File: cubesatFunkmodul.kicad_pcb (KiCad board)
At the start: 4 copper layers, 85 x 85 mm, 96 parts, among them Q1 MMBT5401-TP, Q2 AO3414, Q3 MMBT5551-TP, Q4 MMBT5551-TP, Q5 MMBT5551-TP, Q6 MMBT5551-TP, Q7 MMBT5551-TP, Q8 MMBT5551-TP, U1 MC74HC4538A, U3 ATMEGA128-16AU, U4 LTC3113, U5 RFM23BP, Y1 Crystal_GND24

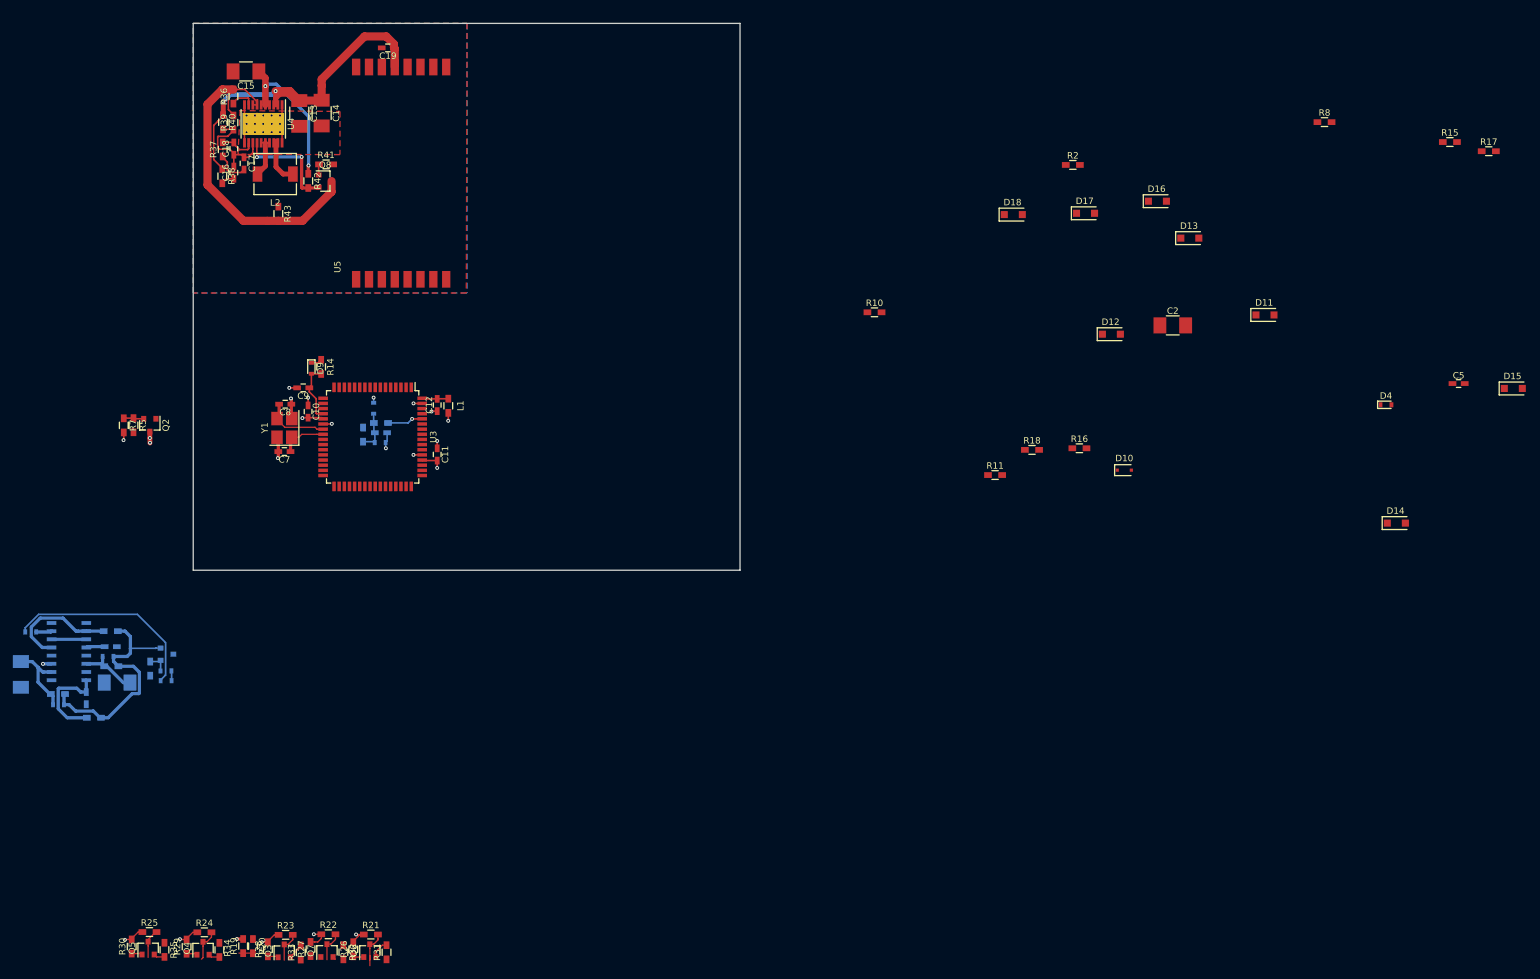
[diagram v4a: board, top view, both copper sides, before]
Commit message: Layout Module1 prefinish
Modules Placed
Ground Plane placed
Supply Plane placed
TODO: Add cubesat connector, Place Antenna connector, Place burnwire connector, Review
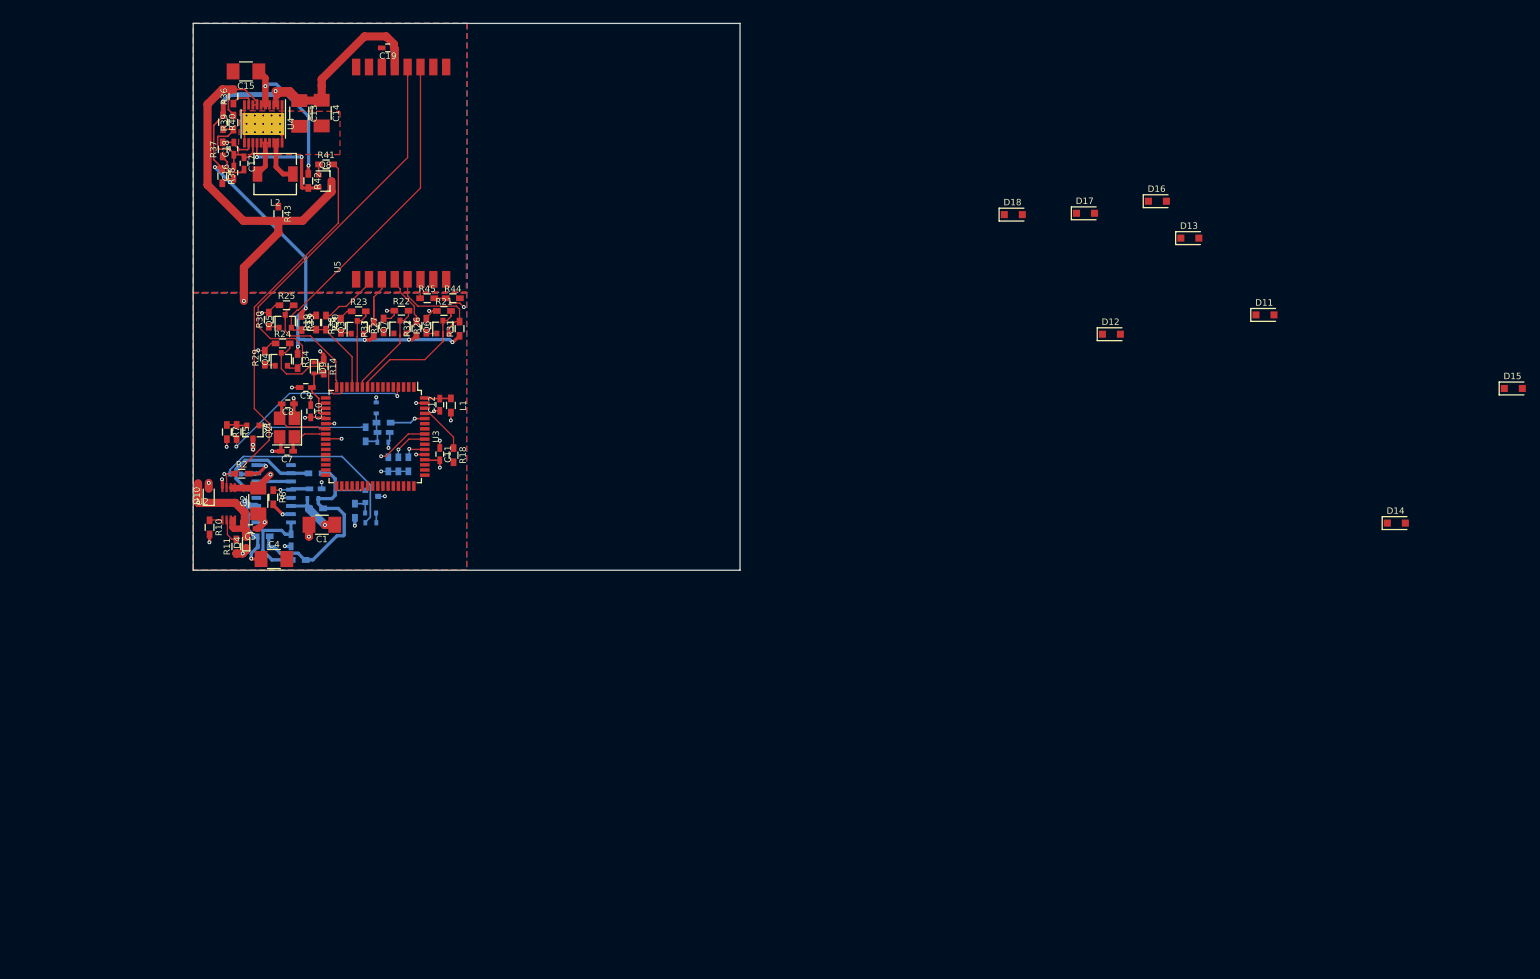
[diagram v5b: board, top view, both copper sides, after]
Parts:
- added R44: 10k, Resistors_SMD:R_0603_HandSoldering, F.Cu at (91.4, 76.7)
- added R45: 4k7, Resistors_SMD:R_0603_HandSoldering, F.Cu at (87.4, 76.7)
- added U2: MAX892, Maxim:µMAX-8, F.Cu at (56.5, 108.6)
- C1, C4: moved to F.Cu
- D1, D2, D3, D4, D5, D6, D7, D8, D9: value STTH102A -> TS4148C
- R15, R16, R17: moved to B.Cu
- moved C5 189.2 mm to (59.9, 112.5), turned to 180 degrees
- moved D4 178.5 mm to (59.2, 114.7), turned to 90 degrees
- moved R17 174.8 mm to (84.5, 102.5), turned to 90 degrees
- moved R8 173.5 mm to (63.4, 107.7), turned to 270 degrees
- moved R15 172.4 mm to (81.3, 102.5), turned to 90 degrees
- moved C2 144.7 mm to (61.1, 108.2), turned to 90 degrees
- moved D10 142.4 mm to (53.4, 107.4), turned to 90 degrees
- moved R2 137.8 mm to (58.5, 104.0)
- moved R11 118.5 mm to (57.7, 115.3), turned to 90 degrees
- moved R10 108.6 mm to (53.5, 112.3), turned to 270 degrees
- moved R16 105.9 mm to (82.9, 102.5), turned to 90 degrees
- moved Q5 99.7 mm to (65.3, 80.3)
- moved R35 99.7 mm to (67.8, 80.6)
- moved R25 99.7 mm to (65.5, 77.8)
- moved R30 99.7 mm to (62.8, 80.1)
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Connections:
- D14 pad 1: (no net) -> /Connector/RX2
- D15 pad 1: (no net) -> /Connector/TX2
- D16 pad 1: (no net) -> /Connector/~ENABLE2~
- R10 pad 1: (no net) -> Net-(R10-Pad1)
- R11 pad 1: (no net) -> /Connector/3.3V
- R11 pad 2: (no net) -> Net-(R11-Pad2)
- U1 pad 9: (no net) -> Net-(U1-Pad9)
- U3 pad 1: (no net) -> Net-(U3-Pad1)
- U3 pad 14: (no net) -> Net-(U3-Pad14)
- U3 pad 17: (no net) -> Net-(U3-Pad17)
- U3 pad 18: (no net) -> Net-(U3-Pad18)
- U3 pad 19: (no net) -> Net-(U3-Pad19)
- U3 pad 26: (no net) -> Net-(U3-Pad26)
- U3 pad 27: (no net) -> Net-(U3-Pad27)
- U3 pad 28: (no net) -> Net-(U3-Pad28)
- U3 pad 29: (no net) -> Net-(U3-Pad29)
- U3 pad 30: (no net) -> Net-(U3-Pad30)
- U3 pad 31: (no net) -> Net-(U3-Pad31)
- U3 pad 32: (no net) -> Net-(U3-Pad32)
- U3 pad 33: (no net) -> Net-(U3-Pad33)
- U3 pad 34: (no net) -> Net-(U3-Pad34)
- U3 pad 35: (no net) -> Net-(U3-Pad35)
- U3 pad 36: (no net) -> Net-(U3-Pad36)
- U3 pad 37: (no net) -> Net-(U3-Pad37)
- U3 pad 38: (no net) -> Net-(U3-Pad38)
- U3 pad 39: (no net) -> Net-(U3-Pad39)
- U3 pad 40: (no net) -> Net-(U3-Pad40)
- U3 pad 41: (no net) -> Net-(U3-Pad41)
- U3 pad 42: (no net) -> Net-(U3-Pad42)
- U3 pad 43: (no net) -> Net-(U3-Pad43)
- U3 pad 44: (no net) -> Net-(U3-Pad44)
- U3 pad 45: (no net) -> Net-(U3-Pad45)
- U3 pad 46: (no net) -> Net-(U3-Pad46)
- U3 pad 47: (no net) -> Net-(U3-Pad47)
- U3 pad 48: (no net) -> Net-(U3-Pad48)
- U3 pad 49: (no net) -> Net-(U3-Pad49)
- U3 pad 5: (no net) -> Net-(U3-Pad5)
- U3 pad 50: (no net) -> Net-(U3-Pad50)
- U3 pad 51: (no net) -> Net-(U3-Pad51)
- U3 pad 55: (no net) -> /Funkmodul1/TDO
- U3 pad 58: (no net) -> Net-(U3-Pad58)
- U3 pad 6: (no net) -> Net-(U3-Pad6)
- U3 pad 62: (no net) -> Net-(U3-Pad62)
- U3 pad 7: (no net) -> Net-(U3-Pad7)
- U3 pad 8: (no net) -> Net-(U3-Pad8)
- U3 pad 9: (no net) -> Net-(U3-Pad9)
- U5 pad 14: (no net) -> Net-(U5-Pad14)
- U5 pad 15: (no net) -> Net-(U5-Pad15)
- U5 pad 16: (no net) -> Net-(U5-Pad16)
- U5 pad 6: /Funkmodul1/Funkeinheit/NIRQ -> /Funkmodul1/Funkeinheit/NIRQ_
- U5 pad 7: GND -> /Funkmodul1/Funkeinheit/PGND
- U5 pad 9: (no net) -> Net-(AE1-Pad1)
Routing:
- net /Funkmodul1/Funkeinheit/5V: track 56.9 -> 123.9 mm, vias 2 -> 8
- net /Funkmodul1/Funkeinheit/RXON_: track 1.74 -> 65.1 mm
- net /Funkmodul1/~ON~: track 31.4 -> 93.3 mm, vias 0 -> 1
- net /Connector/3.3V: track 1.33 -> 53.5 mm, vias 1 -> 6
- net /Funkmodul1/Funkeinheit/TXON_: track 1.75 -> 50.7 mm
- net /Funkmodul1/Funkeinheit/NIRQ: track 0.00 -> 36.3 mm, vias 0 -> 2
- net GND: track 75.3 -> 110.8 mm, vias 14 -> 24
- net /Funkmodul1/BURNWIRE: track 0.00 -> 31.3 mm, vias 0 -> 2
- net /Funkmodul1/VCC: track 27.4 -> 52.4 mm, vias 9 -> 12
- net WIRE_CONN: track 0.04 -> 16.7 mm, vias 0 -> 1
- net /Funkmodul1/Funkeinheit/SS: track 6.39 -> 21.5 mm
- net /Funkmodul1/Funkeinheit/RXON: track 5.17 -> 19.6 mm
- net /Funkmodul1/Funkeinheit/SS_: track 2.91 -> 17.0 mm
- net /Funkmodul1/Funkeinheit/TXON: track 4.56 -> 18.5 mm
- net /Funkmodul1/Funkeinheit/MISO: track 2.44 -> 13.0 mm
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- added copper zone on In2.Cu, net /Funkmodul1/VCC
- added copper zone on B.Cu, net GND
- added copper zone on In1.Cu, net GND

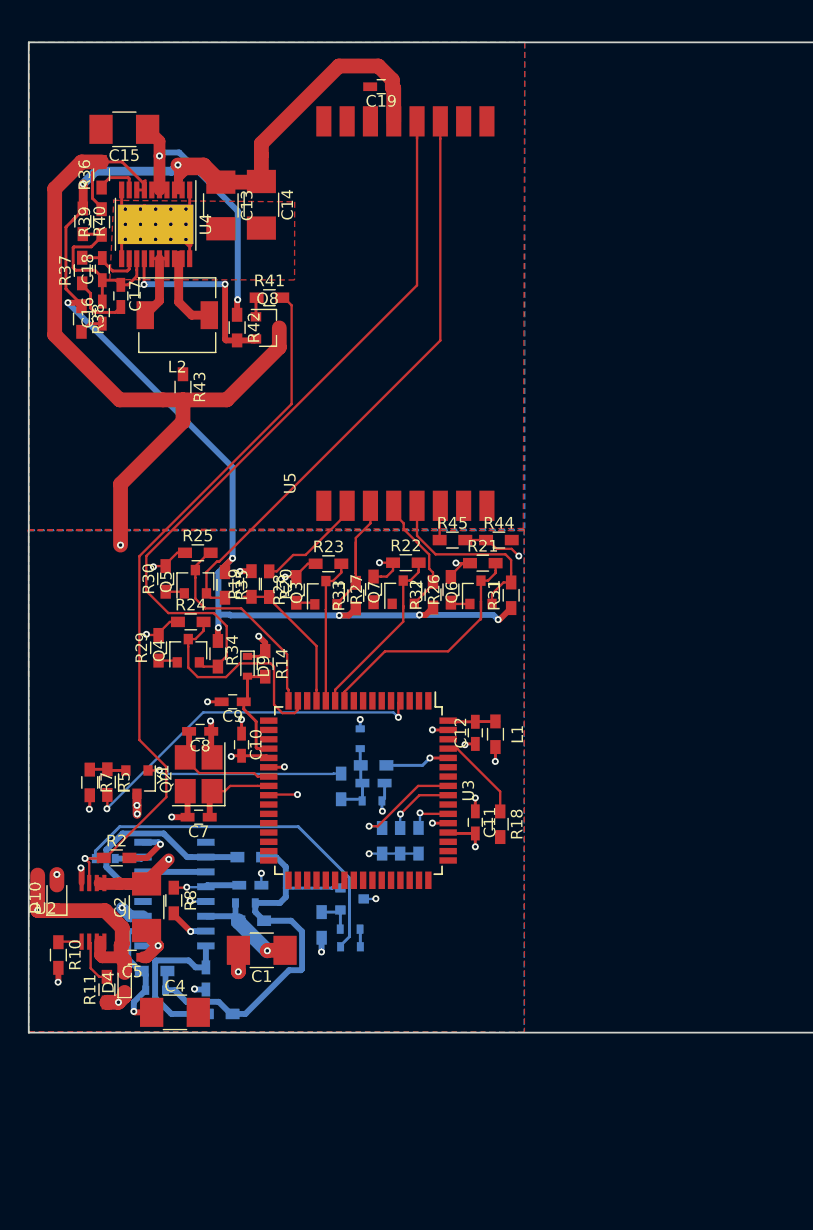
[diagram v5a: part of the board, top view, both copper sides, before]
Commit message: Adds Cubesat Connector to Layout
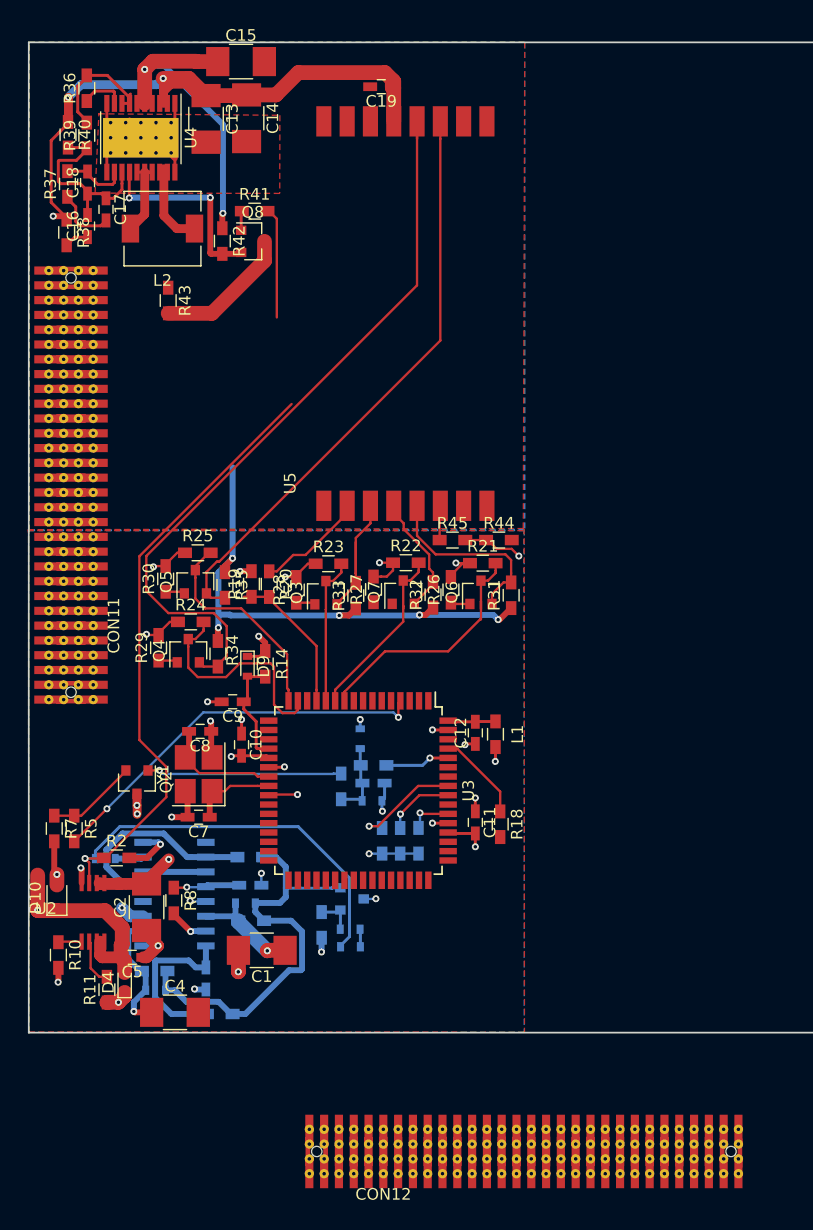
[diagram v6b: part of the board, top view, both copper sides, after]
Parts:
- added CON11: DISCO-CON, cubesatFunkmodul:Cubesatconnector, F.Cu at (54.5, 72.0)
- added CON12: DISCO-CON, cubesatFunkmodul:Cubesatconnector, F.Cu at (93.5, 129.1)
- moved C15 11.6 mm to (69.2, 35.6), turned to 0 degrees
- moved C14 7.54 mm to (69.7, 40.5)
- moved C13 7.54 mm to (66.2, 40.6)
- moved C16 7.54 mm to (56.0, 49.8)
- moved C17 7.54 mm to (57.6, 48.3)
- moved C18 7.54 mm to (56.0, 46.0)
- moved R36 7.54 mm to (56.0, 37.9)
- moved R41 7.54 mm to (70.4, 48.5)
- moved R43 7.54 mm to (63.0, 56.2)
- moved L2 7.54 mm to (62.5, 50.0)
- moved Q8 7.54 mm to (70.2, 51.1)
- moved R37 7.54 mm to (54.3, 46.2)
- moved R38 7.54 mm to (54.3, 50.3)
- moved R39 7.54 mm to (56.0, 42.0)
- moved R40 7.54 mm to (54.4, 41.9)
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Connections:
- D14 pad 1: /Connector/RX2 -> (no net)
- D15 pad 1: /Connector/TX2 -> (no net)
- D16 pad 1: /Connector/~ENABLE2~ -> (no net)
- U1 pad 9: Net-(U1-Pad9) -> (no net)
- U3 pad 1: Net-(U3-Pad1) -> (no net)
- U3 pad 14: Net-(U3-Pad14) -> (no net)
- U3 pad 17: Net-(U3-Pad17) -> (no net)
- U3 pad 18: Net-(U3-Pad18) -> (no net)
- U3 pad 19: Net-(U3-Pad19) -> (no net)
- U3 pad 26: Net-(U3-Pad26) -> (no net)
- U3 pad 27: Net-(U3-Pad27) -> (no net)
- U3 pad 28: Net-(U3-Pad28) -> (no net)
- U3 pad 29: Net-(U3-Pad29) -> (no net)
- U3 pad 30: Net-(U3-Pad30) -> (no net)
- U3 pad 31: Net-(U3-Pad31) -> (no net)
- U3 pad 32: Net-(U3-Pad32) -> (no net)
- U3 pad 33: Net-(U3-Pad33) -> (no net)
- U3 pad 34: Net-(U3-Pad34) -> (no net)
- U3 pad 35: Net-(U3-Pad35) -> (no net)
- U3 pad 36: Net-(U3-Pad36) -> (no net)
- U3 pad 37: Net-(U3-Pad37) -> (no net)
- U3 pad 38: Net-(U3-Pad38) -> (no net)
- U3 pad 39: Net-(U3-Pad39) -> (no net)
- U3 pad 40: Net-(U3-Pad40) -> (no net)
- U3 pad 41: Net-(U3-Pad41) -> (no net)
- U3 pad 42: Net-(U3-Pad42) -> (no net)
- U3 pad 43: Net-(U3-Pad43) -> (no net)
- U3 pad 44: Net-(U3-Pad44) -> (no net)
- U3 pad 45: Net-(U3-Pad45) -> (no net)
- U3 pad 46: Net-(U3-Pad46) -> (no net)
- U3 pad 47: Net-(U3-Pad47) -> (no net)
- U3 pad 48: Net-(U3-Pad48) -> (no net)
- U3 pad 49: Net-(U3-Pad49) -> (no net)
- U3 pad 5: Net-(U3-Pad5) -> (no net)
- U3 pad 50: Net-(U3-Pad50) -> (no net)
- U3 pad 51: Net-(U3-Pad51) -> (no net)
- U3 pad 55: /Funkmodul1/TDO -> (no net)
- U3 pad 58: Net-(U3-Pad58) -> (no net)
- U3 pad 6: Net-(U3-Pad6) -> (no net)
- U3 pad 62: Net-(U3-Pad62) -> (no net)
- U3 pad 7: Net-(U3-Pad7) -> (no net)
- U3 pad 8: Net-(U3-Pad8) -> (no net)
- U3 pad 9: Net-(U3-Pad9) -> (no net)
- U5 pad 14: Net-(U5-Pad14) -> (no net)
- U5 pad 15: Net-(U5-Pad15) -> (no net)
- U5 pad 16: Net-(U5-Pad16) -> (no net)
- U5 pad 9: Net-(AE1-Pad1) -> (no net)
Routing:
- net GND: track 110.8 -> 67.0 mm, vias 24 -> 22
- net /Funkmodul1/Funkeinheit/5V: track 123.9 -> 100.5 mm
- net Net-(Q2-Pad2): track 3.12 -> 7.79 mm
- net VBAT: track 25.2 -> 29.0 mm
- net /Funkmodul1/BURNWIRE: track 31.3 -> 34.1 mm
